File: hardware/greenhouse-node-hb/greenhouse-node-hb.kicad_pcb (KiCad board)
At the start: 4 copper layers, 70 x 50 mm, 39 parts, among them J1 Conn_01x02_Pin, J4 Conn_01x02_Pin, J5 Conn_01x04_Pin, SW1 SW_Push, U1 XC6706x, U3 PCF8574ATS/3,118, U5 L7810, U6 STM32F030F4P6, U7 RFM69HW, U8 A4952ELYTR-T

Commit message: Finish PCB for TS, and renamed boards
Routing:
- net (no net): track 0.00 -> 21.3 mm
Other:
- board text added: "Greenhouse Node HB (Mini)"
- board text added: "Nick Bolton - Rev 2"
- board text removed: "Greenhouse Node Mini - Rev 2"
- board text removed: "Nick Bolton"
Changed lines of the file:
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@@
 (kicad_pcb (version 20221018) (generator pcbnew)
   (general
-    (thickness 4.69)
+    (thickness 1.6)
   )
   (paper "A5")
   (title_block
-    (title "Greenhouse Node Mini")
+    (title "Greenhouse Node HB (Mini)")
     (date "2022-11-16")
     (rev "2")
@@
       (layer "F.Mask" (type "Top Solder Mask") (thickness 0.01))
       (layer "F.Cu" (type "copper") (thickness 0.035))
-      (layer "dielectric 1" (type "core") (thickness 1.51) (material "FR4") (epsilon_r 4.5) (loss_tangent 0.02))
+      (layer "dielectric 1" (type "prepreg") (thickness 0.1) (material "FR4") (epsilon_r 4.5) (loss_tangent 0.02))
       (layer "In1.Cu" (type "copper") (thickness 0.035))
-      (layer "dielectric 2" (type "prepreg") (thickness 1.51) (material "FR4") (epsilon_r 4.5) (loss_tangent 0.02))
+      (layer "dielectric 2" (type "core") (thickness 1.24) (material "FR4") (epsilon_r 4.5) (loss_tangent 0.02))
       (layer "In2.Cu" (type "copper") (thickness 0.035))
-      (layer "dielectric 3" (type "core") (thickness 1.51) (material "FR4") (epsilon_r 4.5) (loss_tangent 0.02))
+      (layer "dielectric 3" (type "prepreg") (thickness 0.1) (material "FR4") (epsilon_r 4.5) (loss_tangent 0.02))
       (layer "B.Cu" (type "copper") (thickness 0.035))
       (layer "B.Mask" (type "Bottom Solder Mask") (thickness 0.01))
@@
   (gr_rect (start 85.86 45.339) (end 126.5 49.784)
     (stroke (width 0.15) (type default)) (fill none) (layer "Dwgs.User"))
-  (gr_rect (start 89.154 53.467) (end 69.85 72.771)
+  (gr_rect (start 69.85 53.467) (end 89.154 72.771)
     (stroke (width 0.15) (type default)) (fill none) (layer "Dwgs.User"))
   (gr_rect locked (start 66 37) (end 136 87)
@@
     (effects (font (size 1 1) (thickness 0.15)))
   )
-  (gr_text "Nick Bolton" (at 134.366 61.849 90) (layer "F.SilkS")
+  (gr_text "Nick Bolton - Rev 2" (at 134.62 61.849 90) (layer "F.SilkS")
     (effects (font (size 1 1) (thickness 0.15)))
   )
@@
     (effects (font (size 1 1) (thickness 0.15)))
   )
-  (gr_text "Greenhouse Node Mini - Rev 2" (at 67.818 61.976 90) (layer "F.SilkS")
+  (gr_text "Greenhouse Node HB (Mini)" (at 67.564 61.976 90) (layer "F.SilkS")
     (effects (font (size 1 1) (thickness 0.15)))
   )
@@
     (effects (font (size 1 1) (thickness 0.15)) (justify left bottom))
   )
+  (segment (start 115.615 83.013) (end 119.550604 83.013) (width 0.25) (layer "F.Cu") (net 0))
+  (segment (start 119.550604 78.697792) (end 128.466 69.782396) (width 0.25) (layer "F.Cu") (net 0))
+  (segment (start 115.316 83.312) (end 115.615 83.013) (width 0.25) (layer "F.Cu") (net 0))
+  (segment (start 119.550604 83.013) (end 119.550604 78.697792) (width 0.25) (layer "F.Cu") (net 0))
   (segment (start 120.777 56.080459) (end 120.777 56.769) (width 0.25) (layer "F.Cu") (net 1))
   (segment (start 120.777 66.548) (end 121.427 66.548) (width 0.25) (layer "F.Cu") (net 1))

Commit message: Tweaks to nodes
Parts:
- added D8: BAT46, Diode_THT:D_DO-35_SOD27_P7.62mm_Horizontal, F.Cu at (98.6, 50.0)
- added J2: Conn_01x03, Jumper:SolderJumper-3_P1.3mm_Bridged2Bar12_RoundedPad1.0x1.5mm, F.Cu at (99.1, 47.5)
- moved D1 3.42 mm to (95.8, 50.0)
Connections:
- C1 pad 2: Net-(D1-K) -> Net-(J2-Pin_2)
- C4 pad 2: Net-(J4-Pin_1) -> +12V
- D1 pad 2: +10V -> +12V
- J4 pad 1: Net-(J4-Pin_1) -> +12V
- U1 pad 3: Net-(D1-K) -> Net-(J2-Pin_2)
- U5 pad 1: Net-(J4-Pin_1) -> +12V
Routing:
- net +12V: track 0.00 -> 29.3 mm
- net Net-(J4-Pin_1): track 26.0 -> 0.00 mm
- net (no net): track 21.3 -> 0.00 mm
- net Net-(J2-Pin_2): track 0.00 -> 7.77 mm
- net Net-(D1-K): track 8.92 -> 4.10 mm
- net Net-(D8-K): track 0.00 -> 4.03 mm
- net +10V: track 44.1 -> 41.3 mm

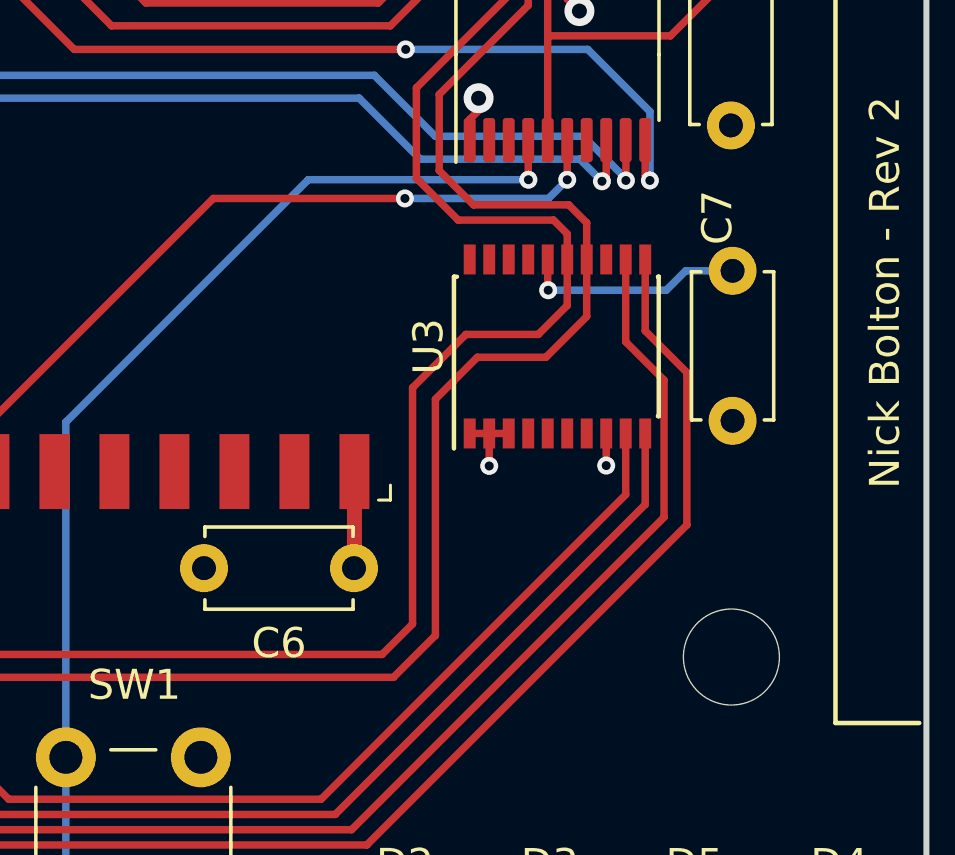
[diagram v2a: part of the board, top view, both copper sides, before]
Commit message: Fixed cap sizes, generated BOMs
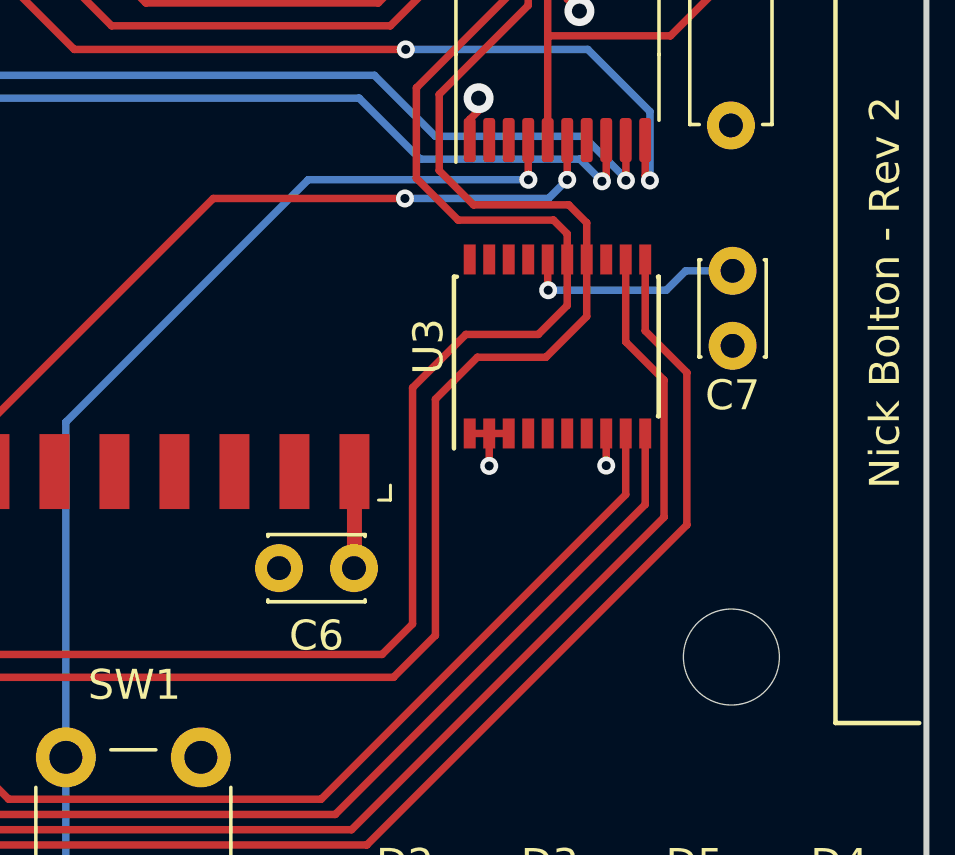
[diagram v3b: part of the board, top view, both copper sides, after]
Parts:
- C6, C7: footprint Capacitor_THT:C_Disc_D4.7mm_W2.5mm_P5.00mm -> Capacitor_THT:C_Disc_D3.0mm_W2.0mm_P2.50mm

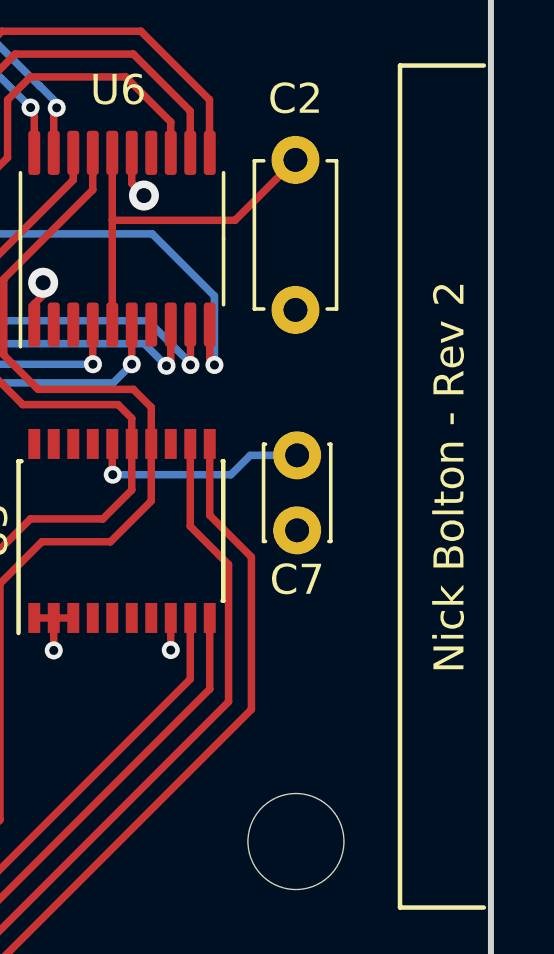
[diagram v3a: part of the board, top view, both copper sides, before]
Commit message: Improved schematics
Add todos, test points, fixed PCF8574 symbol,
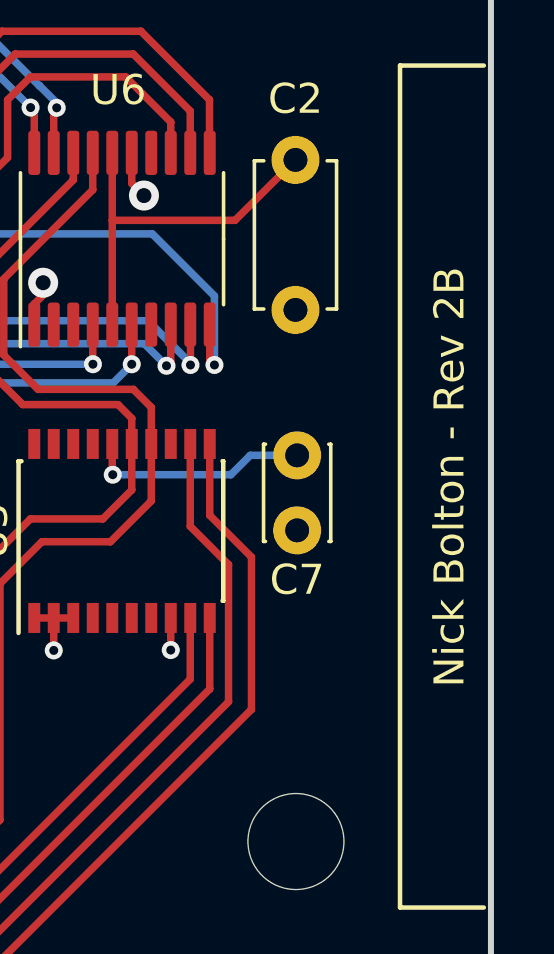
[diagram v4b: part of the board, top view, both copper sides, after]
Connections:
- U3 pad 1: GND -> unconnected-(U3-~{INT}-Pad1)
- U3 pad 10: /LED_R -> unconnected-(U3-P0-Pad10)
- U3 pad 11: /LED_Y -> unconnected-(U3-P1-Pad11)
- U3 pad 12: /LED_B -> unconnected-(U3-P2-Pad12)
- U3 pad 14: /SCL -> unconnected-(U3-P3-Pad14)
- U3 pad 15: /SDA -> GND
- U3 pad 16: +3V3 -> /LED_G
- U3 pad 17: (no net) -> /LED_R
- U3 pad 18: (no net) -> unconnected-(U3-NC-Pad18)
- U3 pad 19: (no net) -> /LED_Y
- U3 pad 2: GND -> /SCL
- U3 pad 20: (no net) -> /LED_B
- U3 pad 3: GND -> unconnected-(U3-NC-Pad3)
- U3 pad 4: unconnected-(U3-P0-Pad4) -> /SDA
- U3 pad 5: unconnected-(U3-P1-Pad5) -> +3V3
- U3 pad 6: unconnected-(U3-P2-Pad6) -> GND
- U3 pad 7: unconnected-(U3-P3-Pad7) -> GND
- U3 pad 8: GND -> unconnected-(U3-NC-Pad8)
- U3 pad 9: /LED_G -> GND
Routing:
- net unconnected-(U3-NC-Pad8): track 0.00 -> 1.07 mm, vias 0 -> 1
- net GND: track 13.7 -> 12.7 mm, vias 20 -> 19
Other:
- board text added: "Nick Bolton - Rev 2B"
- board text removed: "Nick Bolton - Rev 2"
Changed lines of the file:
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@@
   (title_block
     (title "Greenhouse Node HB (Mini)")
-    (date "2022-11-16")
-    (rev "2")
+    (date "2023-05-14")
+    (rev "2B")
     (company "Nick Bolton")
   )
@@
   (net 23 "/RST")
   (net 24 "/M_IN2")
-  (net 25 "unconnected-(U3-P2-Pad6)")
-  (net 26 "unconnected-(U3-P3-Pad7)")
+  (net 25 "unconnected-(U3-~{INT}-Pad1)")
+  (net 26 "unconnected-(U3-NC-Pad3)")
   (net 27 "/RM_IRQ")
   (net 28 "/RM_CS")
   (net 29 "/SCK")
-  (net 30 "unconnected-(U3-P0-Pad4)")
-  (net 31 "unconnected-(U3-P1-Pad5)")
-  (net 32 "unconnected-(U3-~{INT}-Pad13)")
+  (net 30 "unconnected-(U3-NC-Pad8)")
+  (net 31 "unconnected-(U3-P0-Pad10)")
+  (net 32 "unconnected-(U3-P1-Pad11)")
   (net 33 "/MISO")
   (net 34 "/MOSI")
@@
   (net 50 "Net-(D8-K)")
   (net 51 "Net-(#FLG03-pwr)")
+  (net 52 "unconnected-(U3-P2-Pad12)")
+  (net 53 "unconnected-(U3-NC-Pad13)")
+  (net 54 "unconnected-(U3-P3-Pad14)")
+  (net 55 "unconnected-(U3-NC-Pad18)")
   (footprint "Connector_Molex:Molex_KK-254_AE-6410-02A_1x02_P2.54mm_Vertical" (layer "F.Cu")
     (at 78.105 42.164)
@@
     (property "Sheetfile" "greenhouse-node-hb.kicad_sch")
     (property "Sheetname" "")
-    (property "ki_description" "8 Bit Port/Expander to I2C Bus, DIP/SOIC-16")
+    (property "ki_description" "8 Bit Port/Expander to I2C Bus, SSOP-20")
     (property "ki_keywords" "I2C Expander")
     (attr smd)
@@
       (stroke (width 0.15) (type solid)) (layer "F.Fab"))
     (pad "1" smd rect (at -2.9 -2.925 90) (size 1 0.4) (layers "F.Cu" "F.Paste" "F.Mask")
-      (net 1 "GND") (pinfunction "A0") (pintype "input"))
+      (net 25 "unconnected-(U3-~{INT}-Pad1)") (pinfunction "~{INT}") (pintype "open_collector+no_connect"))
     (pad "2" smd rect (at -2.9 -2.275 90) (size 1 0.4) (layers "F.Cu" "F.Paste" "F.Mask")
-      (net 1 "GND") (pinfunction "A1") (pintype "input"))
+      (net 7 "/SCL") (pinfunction "SCL") (pintype "input"))
     (pad "3" smd rect (at -2.9 -1.625 90) (size 1 0.4) (layers "F.Cu" "F.Paste" "F.Mask")
-      (net 1 "GND") (pinfunction "A2") (pintype "input"))
+      (net 26 "unconnected-(U3-NC-Pad3)") (pinfunction "NC") (pintype "no_connect"))
     (pad "4" smd rect (at -2.9 -0.975 90) (size 1 0.4) (layers "F.Cu" "F.Paste" "F.Mask")
-      (net 30 "unconnected-(U3-P0-Pad4)") (pinfunction "P0") (pintype "bidirectional+no_connect"))
+      (net 21 "/SDA") (pinfunction "SDA") (pintype "bidirectional"))
     (pad "5" smd rect (at -2.9 -0.325 90) (size 1 0.4) (layers "F.Cu" "F.Paste" "F.Mask")
-      (net 31 "unconnected-(U3-P1-Pad5)") (pinfunction "P1") (pintype "bidirectional+no_connect"))
+      (net 3 "+3V3") (pinfunction "VDD") (pintype "power_in"))
     (pad "6" smd rect (at -2.9 0.325 90) (size 1 0.4) (layers "F.Cu" "F.Paste" "F.Mask")
-      (net 25 "unconnected-(U3-P2-Pad6)") (pinfunction "P2") (pintype "bidirectional+no_connect"))
+      (net 1 "GND") (pinfunction "A0") (pintype "input"))
     (pad "7" smd rect (at -2.9 0.975 90) (size 1 0.4) (layers "F.Cu" "F.Paste" "F.Mask")
-      (net 26 "unconnected-(U3-P3-Pad7)") (pinfunction "P3") (pintype "bidirectional+no_connect"))
+      (net 1 "GND") (pinfunction "A1") (pintype "input"))
     (pad "8" smd rect (at -2.9 1.625 90) (size 1 0.4) (layers "F.Cu" "F.Paste" "F.Mask")
-      (net 1 "GND") (pinfunction "VSS") (pintype "power_in"))
+      (net 30 "unconnected-(U3-NC-Pad8)") (pinfunction "NC") (pintype "no_connect"))
     (pad "9" smd rect (at -2.9 2.275 90) (size 1 0.4) (layers "F.Cu" "F.Paste" "F.Mask")
-      (net 8 "/LED_G") (pinfunction "P4") (pintype "bidirectional"))
+      (net 1 "GND") (pinfunction "A2") (pintype "input"))
     (pad "10" smd rect (at -2.9 2.925 90) (size 1 0.4) (layers "F.Cu" "F.Paste" "F.Mask")
-      (net 10 "/LED_R") (pinfunction "P5") (pintype "bidirectional"))
+      (net 31 "unconnected-(U3-P0-Pad10)") (pinfunction "P0") (pintype "bidirectional+no_connect"))
     (pad "11" smd rect (at 2.9 2.925 90) (size 1 0.4) (layers "F.Cu" "F.Paste" "F.Mask")
-      (net 12 "/LED_Y") (pinfunction "P6") (pintype "bidirectional"))
+      (net 32 "unconnected-(U3-P1-Pad11)") (pinfunction "P1") (pintype "bidirectional+no_connect"))
     (pad "12" smd rect (at 2.9 2.275 90) (size 1 0.4) (layers "F.Cu" "F.Paste" "F.Mask")
-      (net 14 "/LED_B") (pinfunction "P7") (pintype "bidirectional"))
+      (net 52 "unconnected-(U3-P2-Pad12)") (pinfunction "P2") (pintype "bidirectional+no_connect"))
     (pad "13" smd rect (at 2.9 1.625 90) (size 1 0.4) (layers "F.Cu" "F.Paste" "F.Mask")
-      (net 32 "unconnected-(U3-~{INT}-Pad13)") (pinfunction "~{INT}") (pintype "open_collector+no_connect"))
+      (net 53 "unconnected-(U3-NC-Pad13)") (pinfunction "NC") (pintype "no_connect"))
     (pad "14" smd rect (at 2.9 0.975 90) (size 1 0.4) (layers "F.Cu" "F.Paste" "F.Mask")
-      (net 7 "/SCL") (pinfunction "SCL") (pintype "input"))
+      (net 54 "unconnected-(U3-P3-Pad14)") (pinfunction "P3") (pintype "bidirectional+no_connect"))
     (pad "15" smd rect (at 2.9 0.325 90) (size 1 0.4) (layers "F.Cu" "F.Paste" "F.Mask")
-      (net 21 "/SDA") (pinfunction "SDA") (pintype "bidirectional"))
+      (net 1 "GND") (pinfunction "VSS") (pintype "power_in"))
     (pad "16" smd rect (at 2.9 -0.325 90) (size 1 0.4) (layers "F.Cu" "F.Paste" "F.Mask")
-      (net 3 "+3V3") (pinfunction "VDD") (pintype "power_in"))
-    (pad "17" smd rect (at 2.9 -0.975 90) (size 1 0.4) (layers "F.Cu" "F.Paste" "F.Mask"))
-    (pad "18" smd rect (at 2.9 -1.625 90) (size 1 0.4) (layers "F.Cu" "F.Paste" "F.Mask"))
-    (pad "19" smd rect (at 2.9 -2.275 90) (size 1 0.4) (layers "F.Cu" "F.Paste" "F.Mask"))
-    (pad "20" smd rect (at 2.9 -2.925 90) (size 1 0.4) (layers "F.Cu" "F.Paste" "F.Mask"))
+      (net 8 "/LED_G") (pinfunction "P4") (pintype "bidirectional"))
+    (pad "17" smd rect (at 2.9 -0.975 90) (size 1 0.4) (layers "F.Cu" "F.Paste" "F.Mask")
+      (net 10 "/LED_R") (pinfunction "P5") (pintype "bidirectional"))
+    (pad "18" smd rect (at 2.9 -1.625 90) (size 1 0.4) (layers "F.Cu" "F.Paste" "F.Mask")
+      (net 55 "unconnected-(U3-NC-Pad18)") (pinfunction "NC") (pintype "no_connect"))
+    (pad "19" smd rect (at 2.9 -2.275 90) (size 1 0.4) (layers "F.Cu" "F.Paste" "F.Mask")
+      (net 12 "/LED_Y") (pinfunction "P6") (pintype "bidirectional"))
+    (pad "20" smd rect (at 2.9 -2.925 90) (size 1 0.4) (layers "F.Cu" "F.Paste" "F.Mask")
+      (net 14 "/LED_B") (pinfunction "P7") (pintype "bidirectional"))
     (model "${KICAD6_3DMODEL_DIR}/Package_SO.3dshapes/SSOP-20_4.4x6.5mm_P0.65mm.wrl"
       (offset (xyz 0 0 0))
@@
     (effects (font (size 1 1) (thickness 0.15)))
   )
-  (gr_text "Nick Bolton - Rev 2" (at 134.62 61.849 90) (layer "F.SilkS")
+  (gr_text "Nick Bolton - Rev 2B" (at 134.62 61.849 90) (layer "F.SilkS")
     (effects (font (size 1 1) (thickness 0.15)))
   )
@@
   (segment (start 121.427 67.6298) (end 121.427 66.548) (width 0.25) (layer "F.Cu") (net 1))
   (segment (start 124.433766 52.468065) (end 124.027 52.061299) (width 0.25) (layer "F.Cu") (net 1))
-  (segment (start 125.327 67.6182) (end 125.327 66.548) (width 0.25) (layer "F.Cu") (net 1))
   (segment (start 106.524 40.64) (end 104.984 40.64) (width 0.5) (layer "F.Cu") (net 1))
   (segment (start 111.014 40.64) (end 111.047 40.607) (width 0.5) (layer "F.Cu") (net 1))
@@
   (via (at 76.581 46.99) (size 1) (drill 0.5) (layers "F.Cu" "B.Cu") (free) (net 1))
   (via (at 76.581 49.784) (size 1) (drill 0.5) (layers "F.Cu" "B.Cu") (free) (net 1))
-  (via (at 125.327 67.6182) (size 0.6) (drill 0.3) (layers "F.Cu" "B.Cu") (net 1))
   (via (at 121.073501 55.373253) (size 1) (drill 0.5) (layers "F.Cu" "B.Cu") (net 1))
   (via (at 83.312 48.641) (size 1) (drill 0.5) (layers "F.Cu" "B.Cu") (free) (net 1))
@@
   (segment (start 111.246 51.435) (end 117.518 51.435) (width 0.25) (layer "F.Cu") (net 29))
   (segment (start 118.364 50.589) (end 118.364 48.3235) (width 0.25) (layer "F.Cu") (net 29))
+  (segment (start 125.327 67.6182) (end 125.327 66.548) (width 0.25) (layer "F.Cu") (net 30))
+  (via (at 125.327 67.6182) (size 0.6) (drill 0.3) (layers "F.Cu" "B.Cu") (net 30))
   (segment (start 124.079 47.752) (end 120.142 47.752) (width 0.25) (layer "F.Cu") (net 33))
   (segment (start 119.126 50.8) (end 117.729 52.197) (width 0.25) (layer "F.Cu") (net 33))
